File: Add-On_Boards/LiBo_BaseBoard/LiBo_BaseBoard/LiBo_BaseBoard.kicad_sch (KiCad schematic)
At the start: 57 parts, among them IC1 MCP1702T-5002E_MB, IC2 ADS1015IDGSR, IC4 SN74LVC125APWR, J1 USB_C_Receptacle_USB2.0, J10 Conn_01x18, J2 2199230-3, J3 KH-BNC50-3511, J4 KH-BNC50-3511, J5 Conn_01x16, J6 TF_PUSH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

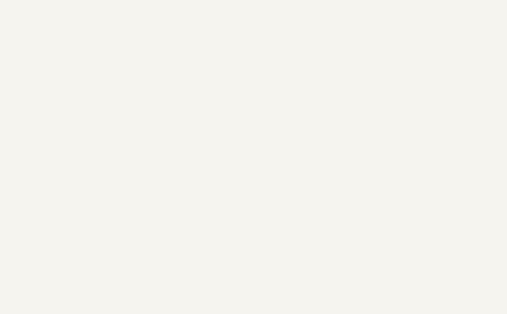
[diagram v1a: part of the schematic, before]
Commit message: Feat: LiBo_M.2_ESP32S3 Added
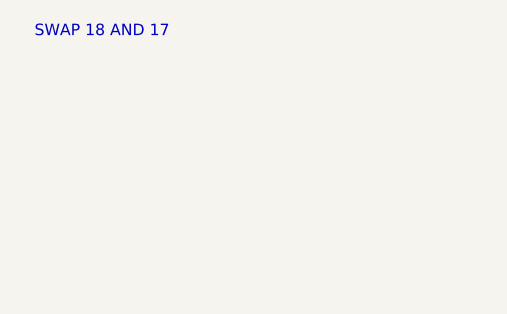
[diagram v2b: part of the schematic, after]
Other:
- note added: "SWAP 18 AND 17"
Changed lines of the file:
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@@
+		)
+	)
+	(text "SWAP 18 AND 17"
+		(exclude_from_sim no)
+		(at -38.862 -12.446 0)
+		(effects
+			(font
+				(size 1.27 1.27)
+			)
 		)
 	)

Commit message: updated the Libo M.2 main board
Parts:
- removed BOOT1: SW_BOOT, Button_Switch_SMD:SW_SPST_EVQP2, symbol Switch:SW_Push
- removed C1, C2: 1u, Capacitor_SMD:C_0805_2012Metric_Pad1.18x1.45mm_HandSolder, symbol Device:C
- removed C10, C13, C5: 10u, Capacitor_SMD:C_0805_2012Metric_Pad1.18x1.45mm_HandSolder, symbol Device:C
- removed C11, C12, C3, C6, C7, C8: 100n, Capacitor_SMD:C_0805_2012Metric_Pad1.18x1.45mm_HandSolder, symbol Device:C
- removed C4, C9: 4u7, Capacitor_SMD:C_0805_2012Metric_Pad1.18x1.45mm_HandSolder, symbol Device:C
- removed D1, D2, D3: LED, LED_SMD:LED_0805_2012Metric_Pad1.15x1.40mm_HandSolder, symbol Device:LED
- removed IC1: MCP1702T-5002E_MB, Github_Library:MCP1703T5002EMB, symbol GitHub_Library:MCP1702T-5002E_MB
- removed IC2: ADS1015IDGSR, Github_Library:SOP50P490X110-10N, symbol GitHub_Library:ADS1015IDGSR
- removed IC4: SN74LVC125APWR, Github_Library:SN74LVC125APWR, symbol GitHub_Library:SN74LVC125APWR
- removed J1: USB_C_Receptacle_USB2.0, Connector_USB:USB_C_Receptacle_GCT_USB4105-xx-A_16P_TopMnt_Horizontal, symbol KiCad_Library:USB_C_Receptacle_USB2.0
- removed J10: Conn_01x18, Connector_PinHeader_2.54mm:PinHeader_1x18_P2.54mm_Horizontal, symbol Connector_Generic:Conn_01x18
- removed J2: 2199230-3, Github_Library:21992303, symbol GitHub_Library:M.2_67Con_Fem_2199230-3
- removed J3, J4: KH-BNC50-3511, Github_Library:KHBNC503511, symbol GitHub_Library:KH-BNC50-3511
- removed J5: Conn_01x16, Connector_PinHeader_2.54mm:PinHeader_1x16_P2.54mm_Vertical, symbol Connector_Generic:Conn_01x16
- removed J6: TF_PUSH, Github_Library:TFPUSH, symbol GitHub_Library:TF_PUSH
- removed J7: Conn_ST_STDC14, Connector_PinHeader_1.27mm:PinHeader_2x07_P1.27mm_Vertical, symbol Connector:Conn_ST_STDC14
- removed J8: Conn_01x10, Connector_PinHeader_2.54mm:PinHeader_1x10_P2.54mm_Vertical, symbol Connector_Generic:Conn_01x10
- removed L1: 2u2, LED_SMD:LED_0805_2012Metric_Pad1.15x1.40mm_HandSolder, symbol Device:L
- removed LED1: WS2812C-2020, Github_Library:WS2812C2020, symbol GitHub_Library:WS2812C-2020
- removed R1, R13, R14, R15, R18, R4, R7: 10k, Resistor_SMD:R_0805_2012Metric_Pad1.20x1.40mm_HandSolder, symbol Device:R
- removed R10, R11, R12, R16, R17, R9: 3k3, Resistor_SMD:R_0805_2012Metric_Pad1.20x1.40mm_HandSolder, symbol Device:R
- removed R19, R2, R20, R21, R3: 5k1, Resistor_SMD:R_0805_2012Metric_Pad1.20x1.40mm_HandSolder, symbol Device:R
- removed R5: 450k, Resistor_SMD:R_0805_2012Metric_Pad1.20x1.40mm_HandSolder, symbol Device:R
- removed R6: 100k, Resistor_SMD:R_0805_2012Metric_Pad1.20x1.40mm_HandSolder, symbol Device:R
- removed R8: 220, Resistor_SMD:R_0805_2012Metric_Pad1.20x1.40mm_HandSolder, symbol Device:R
- removed RST1: SW_RST, Button_Switch_SMD:SW_SPST_EVQP2, symbol Switch:SW_Push
- removed RV1: 10k, Potentiometer_THT:Potentiometer_Bourns_3296W_Vertical, symbol Device:R_Potentiometer
- removed U1: USBLC6-2SC6, Package_TO_SOT_SMD:SOT-23-6, symbol Power_Protection:USBLC6-2SC6
- removed U2: TLV62568DBV, Package_TO_SOT_SMD:SOT-23-5, symbol Regulator_Switching:TLV62568DBV
- removed U3: MCP4725A0T-E/CH, Package_TO_SOT_SMD:SOT-23-6, symbol Analog_DAC:MCP4725xxx-xCH
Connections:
- no-connect marks 8 -> 0
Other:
- added sheet M.2_INPUT (M.2_Input_Page.kicad_sch)
- added sheet OUTPUTS (Outputs_Page.kicad_sch)
- added sheet POWER (Power_Page.kicad_sch)
- added sheet SUB-COMPONENTS (Sub_Components_Page.kicad_sch)
- note removed: "16x2 LCD"
- note removed: "Add comments for Pull-Up Resistors -> I2C"
- note removed: "Analog Digital Converter"
- note removed: "B-Key-Female"
- note removed: "BOOT Button"
- note removed: "Digital Analog Converter"
- note removed: "FOXCONN AS0BC21-S40BB-7H"
- note removed: "GND 1001000 VDD 1001001"
- note removed: "I2C Address: 1001000"
- note removed: "I2C Address: 1100000"
- note removed: "I2C Pull-Up"
- note removed: "I2C USED"
- note removed: "JTAG/SWD"
- note removed: "Logic Level Shifter"
- note removed: "M.2 Connector"
- note removed: "MCU OUT (V) SD IN 3V3"
- note removed: "Micro SDCard"
- note removed: "NON-I2C"
- note removed: "Pull-Up"
- note removed: "RGB Status LED"
- note removed: "RST Button"
- note removed: "SCK (SPI) -> Pull Down Resistor 10K"
- note removed: "SD Card Slot"
- note removed: "SD OUT (V) MCU IN 3V3"
- note removed: "ST-Link Config"
- note removed: "SWAP 18 AND 17"
- note removed: "Shifter for SDCard LOW = ENABLE"
- note removed: "USB 2.0 Umax = 5V Imax = 3A"
- note removed: "USB_C"
- note removed: "USED"
- note removed: "USED FOR TESTING"
- note removed: "USED SPI"
- note removed: "VBUS -> +3V3"
- note removed: "VBUS -> +5V"
- note removed: "Voltage Converter"
- note removed: "WS2812-2020"
- note removed: "Warning, Strapping Pins."
